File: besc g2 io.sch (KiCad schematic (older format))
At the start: 34 parts, among them J10 USB_B_Micro, J11 THROTTLE, J12 MOTOR SENSOR, J13 THROTTLE 2 (BRAKE), J14 SERIAL, J15 IGNITION, J16 CAN, J8 SWD, J9 RC PWM, U10 TJA1051T-3, U9 USBLC6-2SC6

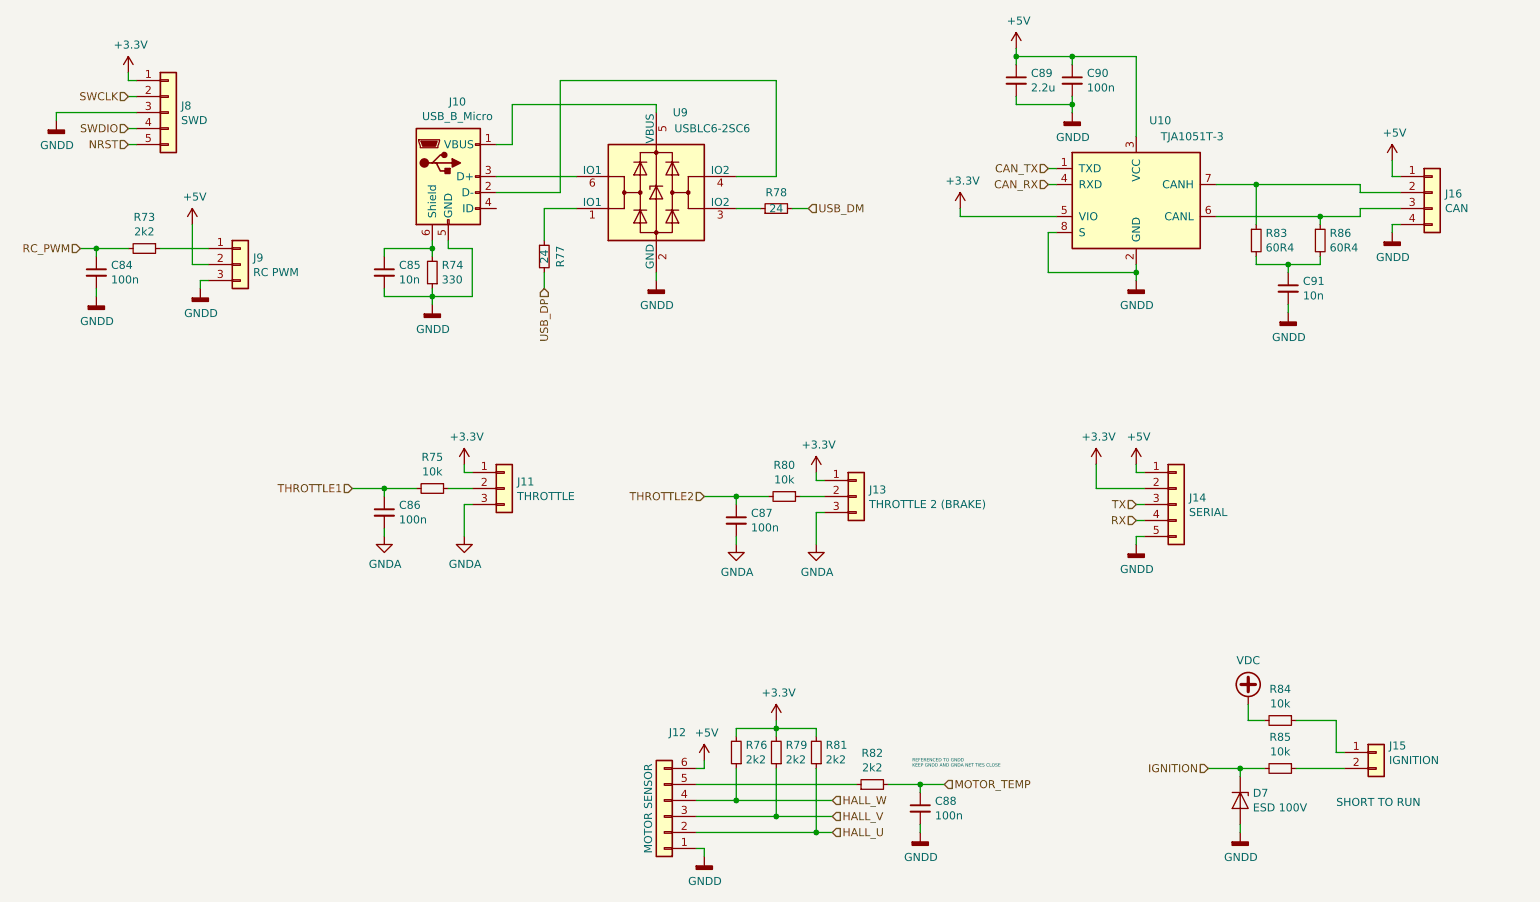
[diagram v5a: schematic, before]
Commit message: finished routing, added bom and step
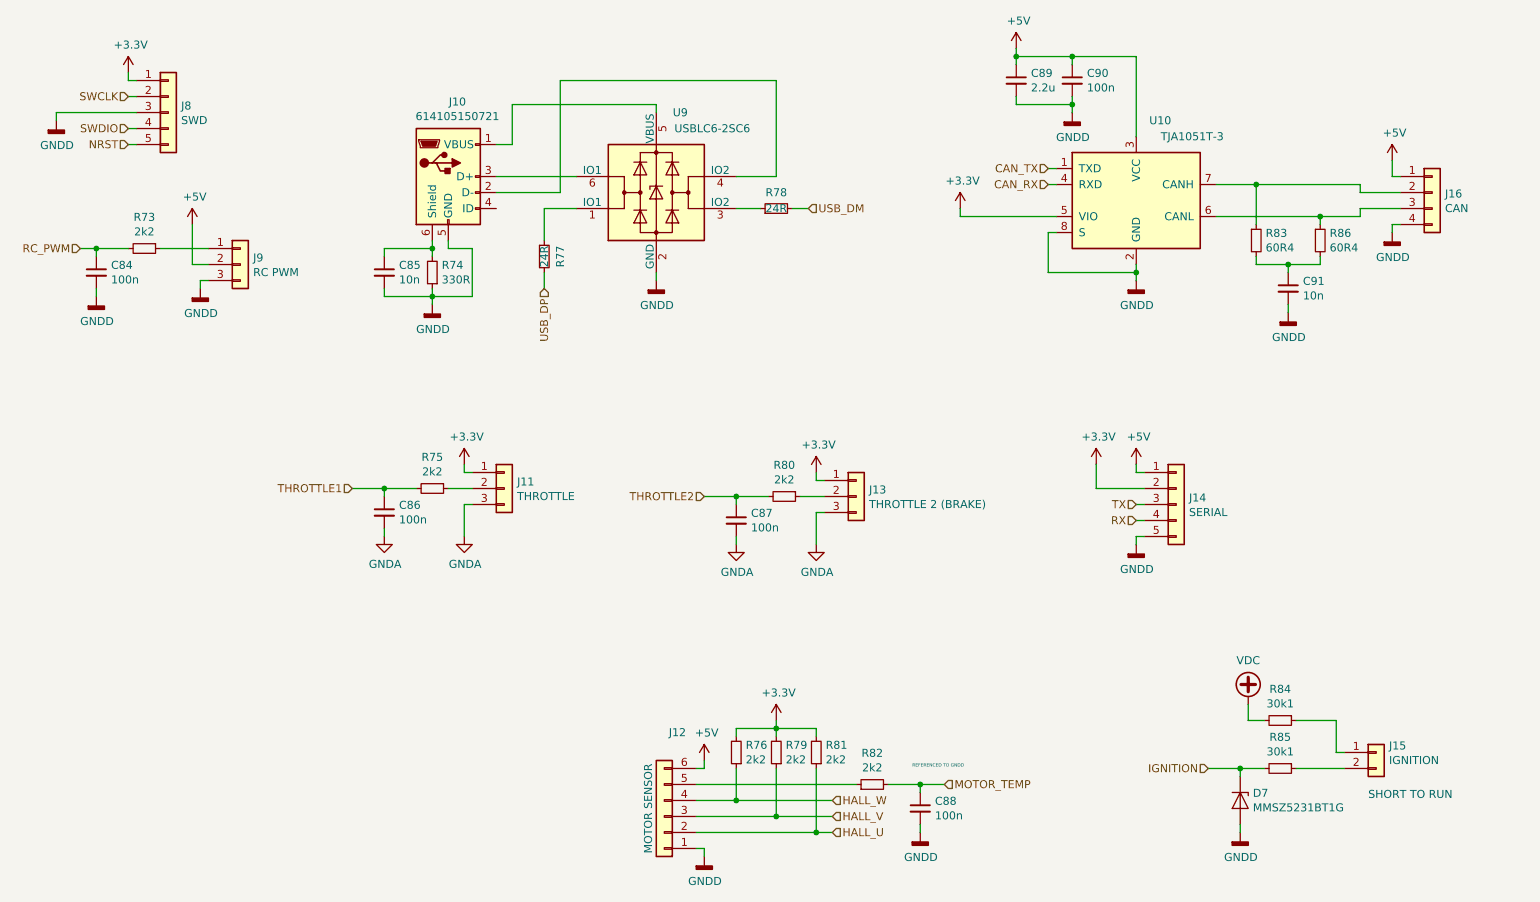
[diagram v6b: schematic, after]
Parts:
- D7: value ESD 100V -> MMSZ5231BT1G
- J10: value USB_B_Micro -> 614105150721
- R74: value 330 -> 330R
- R75, R80: value 10k -> 2k2
- R77, R78: value 24 -> 24R
- R84, R85: value 10k -> 30k1
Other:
- note added: "REFERENCED TO GNDD"
- note removed: "REFERENCED TO GNDD\nKEEP GNDD AND GNDA NET TIES CLOSE"
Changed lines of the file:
@@
 encoding utf-8
 Sheet 4 5
-Title ""
-Date ""
-Rev ""
-Comp ""
+Title "BESC Gen 2"
+Date "14.7.2019"
+Rev "init"
+Comp "e.pavlin.si"
 Comment1 ""
 Comment2 ""
@@
 P 3650 1750
 F 0 "J10" H 3707 2217 50  0000 C CNN
-F 1 "USB_B_Micro" H 3707 2126 50  0000 C CNN
+F 1 "614105150721" H 3707 2126 50  0000 C CNN
 F 2 "Connector_USB:USB_Micro-B_Wuerth_614105150721_Vertical_CircularHoles" H 3800 1700 50  0001 C CNN
 F 3 "~" H 3800 1700 50  0001 C CNN
@@
 P 3550 2350
 F 0 "R74" H 3491 2304 50  0000 R CNN
-F 1 "330" H 3491 2395 50  0000 R CNN
+F 1 "330R" H 3491 2395 50  0000 R CNN
 F 2 "Resistor_SMD:R_0603_1608Metric" H 3550 2350 50  0001 C CNN
 F 3 "~" H 3550 2350 50  0001 C CNN
@@
 P 5700 1950
 F 0 "R78" V 5800 1950 50  0000 C CNN
-F 1 "24" V 5700 1950 50  0000 C CNN
+F 1 "24R" V 5700 1950 50  0000 C CNN
 F 2 "Resistor_SMD:R_0603_1608Metric" H 5700 1950 50  0001 C CNN
 F 3 "~" H 5700 1950 50  0001 C CNN
@@
 P 4250 2250
 F 0 "R77" V 4350 2250 50  0000 C CNN
-F 1 "24" V 4250 2250 50  0000 C CNN
+F 1 "24R" V 4250 2250 50  0000 C CNN
 F 2 "Resistor_SMD:R_0603_1608Metric" H 4250 2250 50  0001 C CNN
 F 3 "~" H 4250 2250 50  0001 C CNN
@@
 P 3550 3700
 F 0 "R75" V 3354 3700 50  0000 C CNN
-F 1 "10k" V 3445 3700 50  0000 C CNN
+F 1 "2k2" V 3445 3700 50  0000 C CNN
 F 2 "Resistor_SMD:R_0603_1608Metric" H 3550 3700 50  0001 C CNN
 F 3 "~" H 3550 3700 50  0001 C CNN
@@
 P 5750 3750
 F 0 "R80" V 5554 3750 50  0000 C CNN
-F 1 "10k" V 5645 3750 50  0000 C CNN
+F 1 "2k2" V 5645 3750 50  0000 C CNN
 F 2 "Resistor_SMD:R_0603_1608Metric" H 5750 3750 50  0001 C CNN
 F 3 "~" H 5750 3750 50  0001 C CNN
@@
 	6600 5800 6600 5850
 Text Notes 6550 5450 0    20   ~ 0
-REFERENCED TO GNDD\nKEEP GNDD AND GNDA NET TIES CLOSE
+REFERENCED TO GNDD
 $Comp
 L Connector_Generic:Conn_01x02 J15
@@
 P 8850 5450
 F 0 "R85" V 8654 5450 50  0000 C CNN
-F 1 "10k" V 8745 5450 50  0000 C CNN
+F 1 "30k1" V 8745 5450 50  0000 C CNN
 F 2 "Resistor_SMD:R_0603_1608Metric" H 8850 5450 50  0001 C CNN
 F 3 "~" H 8850 5450 50  0001 C CNN
@@
 P 8850 5150
 F 0 "R84" V 8654 5150 50  0000 C CNN
-F 1 "10k" V 8745 5150 50  0000 C CNN
+F 1 "30k1" V 8745 5150 50  0000 C CNN
 F 2 "Resistor_SMD:R_0603_1608Metric" H 8850 5150 50  0001 C CNN
 F 3 "~" H 8850 5150 50  0001 C CNN
@@
 P 8600 5650
 F 0 "D7" V 8554 5729 50  0000 L CNN
-F 1 "ESD 100V" V 8645 5729 50  0000 L CNN
+F 1 "MMSZ5231BT1G" V 8645 5729 50  0000 L CNN
 F 2 "Diode_SMD:D_SOD-123" H 8600 5650 50  0001 C CNN
 F 3 "~" H 8600 5650 50  0001 C CNN
@@
 Wire Wire Line
 	8600 5850 8600 5800
-Text Notes 9200 5700 0    50   ~ 0
+Text Notes 9400 5650 0    50   ~ 0
 SHORT TO RUN
 Wire Wire Line
